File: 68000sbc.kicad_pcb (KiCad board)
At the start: 2 copper layers, 127 x 90.8 mm, 49 parts, among them J1 USB_B, J2 5V FTDI SERIAL, J3 RTC (SparkFun BOB-10160), J4 CFCARD/IDE, J5 EXPANSION (F.Cu), J6 EXPANSION (B.Cu), SW1 RESET, SW2 BTN1, U1 74HC139, U2 74HC14, U3 TMP68HC000P-12, U4 AS6C4008-55PCN, U5 28C256, U6 AS6C4008-55PCN, U7 28C256, U8 TL16C550, X1 12MHz, X2 12MHz

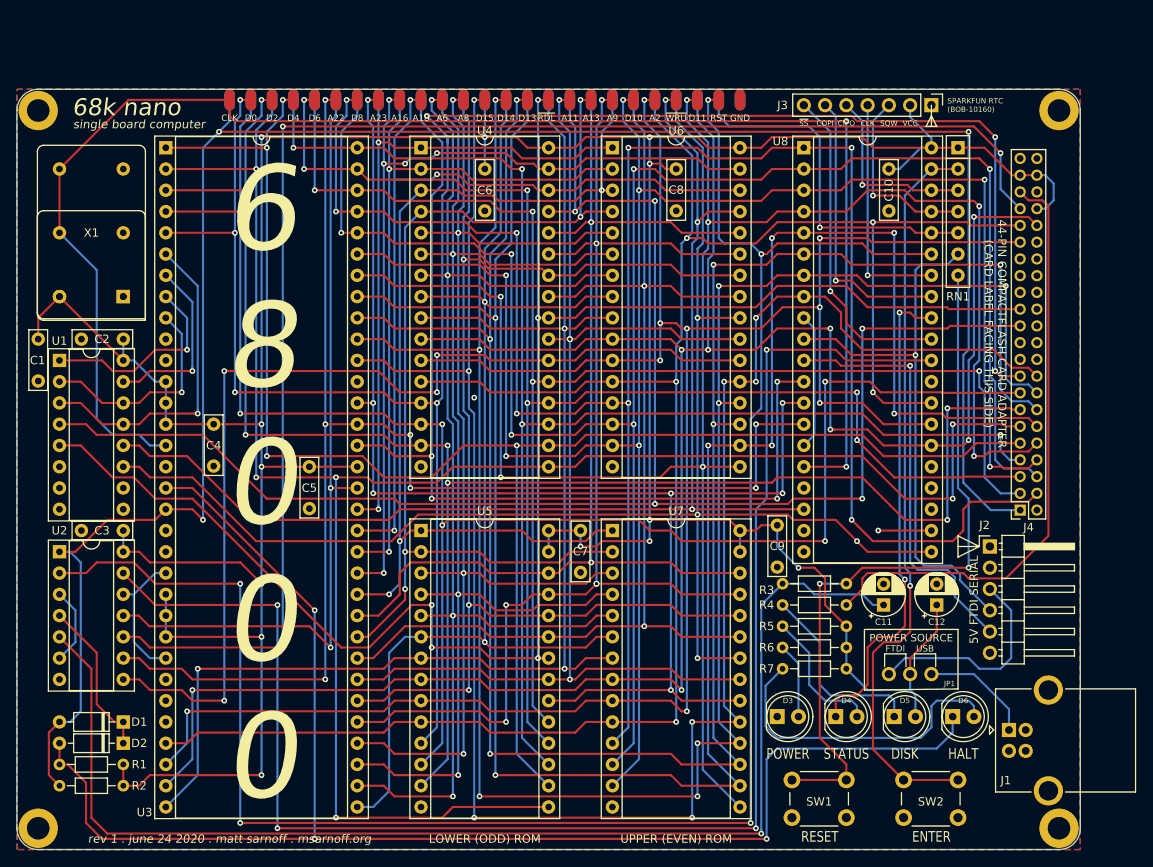
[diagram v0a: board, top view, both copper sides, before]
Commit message: Convert DIP-64 CPU to PGA-68 (MC68HC000RC) on a 4-layer board, fully routed
- New footprint PadRows:MC68HC000_PGA68 (pad numbers = DIP-64 pins, so the
  existing CPU_NXP_68000 symbol works unchanged)
- U3 swapped DIP-64 -> PGA-68; X1/X2 oscillator and J5/J6 headers relocated
  to clear the PGA; top board edge raised 6.4mm
- Board converted to 4 layers: F.Cu/B.Cu signal, In1.Cu GND plane,
  In2.Cu VCC plane (PGA inner-pin escape needs >2 layers)
- Routed with FreeRouting (119/137 nets) + a custom maze router for the
  final 6 spans; DRC: 0 unconnected, 0 copper/electrical violations
- PGA68/ holds the pin map, conversion scripts, and the routing report

Co-Authored-By: Claude Opus 4.8 <noreply@anthropic.com>
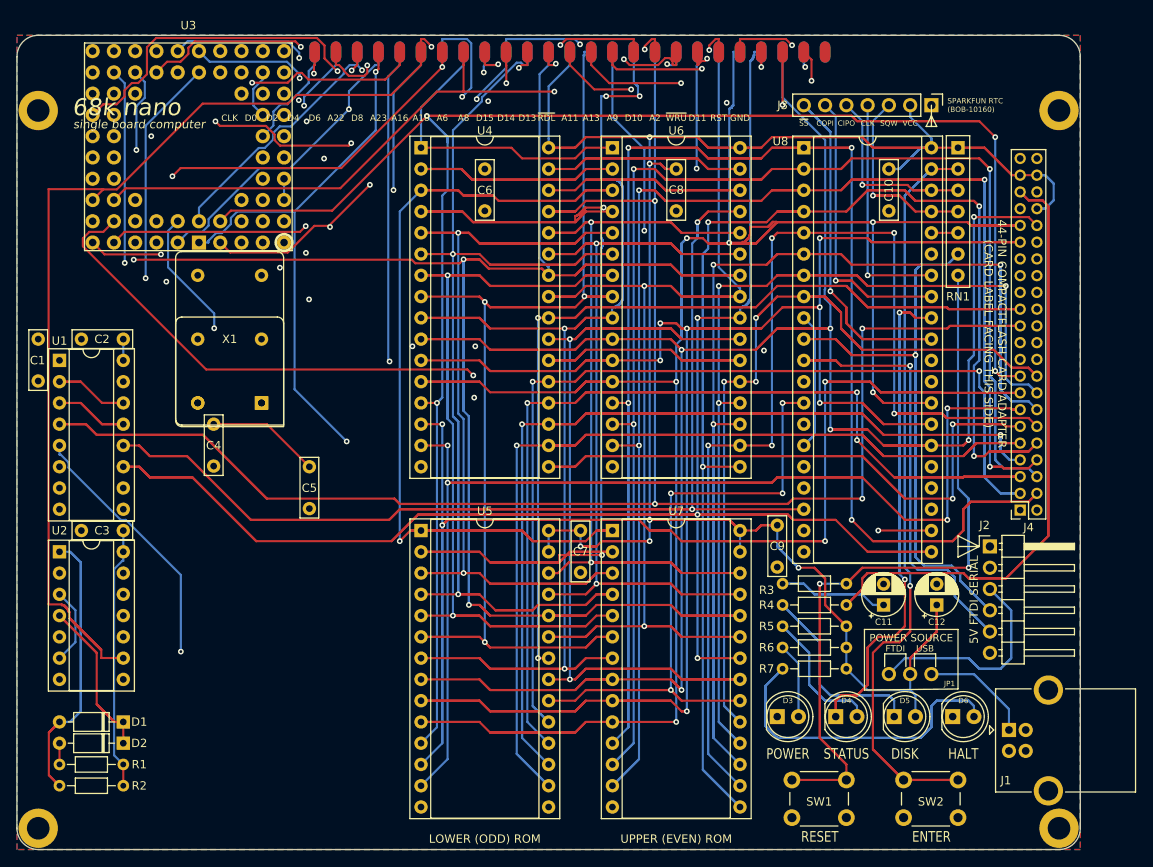
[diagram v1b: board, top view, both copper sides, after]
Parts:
- U3: value TMP68HC000P-12 -> MC68HC000RC10; footprint Package_DIP:DIP-64_W22.86mm_Socket -> PadRows:MC68HC000_PGA68
- moved X1 20.8 mm to (72.4, 76.2)
- moved X2 20.8 mm to (72.4, 76.2)
- moved J5 11.7 mm to (109.2, 38.1)
- moved J6 11.7 mm to (109.2, 30.5)
- moved U3 2.69 mm to (63.6, 45.6)
- renumbered REF** to H1, REF** to H2, REF** to H3, REF** to H4
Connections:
- net /R,~W renamed /R,~{W}
- net /~A20 renamed /~{A20}
- net /~A22 renamed /~{A22}
- net /~AS renamed /~{AS}
- net /~BTN1 renamed /~{BTN1}
- net /~CFLED renamed /~{CFLED}
- net /~HALT renamed /~{HALT}
- net /~IRQ renamed /~{IRQ}
- net /~LDS renamed /~{LDS}
- net /~RDL renamed /~{RDL}
- net /~RDU renamed /~{RDU}
- net /~RESET renamed /~{RESET}
- net /~RESETBTN renamed /~{RESETBTN}
- net /~RTC_SS renamed /~{RTC_SS}
- net /~UDS renamed /~{UDS}
- net /~WRL renamed /~{WRL}
- net /~WRU renamed /~{WRU}
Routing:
- net /A10: track 154.0 -> 288.0 mm, vias 3 -> 4
- net /A2: track 256.3 -> 378.3 mm
- net /A1: track 240.6 -> 352.6 mm, vias 5 -> 6
- net /A11: track 142.7 -> 251.9 mm, vias 4 -> 6
- net /D5: track 169.9 -> 277.6 mm, vias 4 -> 3
- net /D11: track 230.8 -> 337.5 mm, vias 7 -> 5
- net /A3: track 260.8 -> 363.2 mm, vias 8 -> 7
- net /~{WRL}: track 202.4 -> 303.4 mm, vias 5 -> 4
- net /D7: track 171.5 -> 272.3 mm
- net /A15: track 116.5 -> 216.1 mm, vias 3 -> 2
- net /A14: track 130.6 -> 225.0 mm, vias 2 -> 3
- net /D10: track 225.6 -> 319.2 mm, vias 7 -> 6
- net /A13: track 119.7 -> 212.6 mm, vias 4 -> 5
- net /D8: track 244.3 -> 336.6 mm, vias 8 -> 6
- net /A12: track 136.2 -> 226.3 mm, vias 2 -> 3
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- added copper zone on In1.Cu, net GND
- added copper zone on In2.Cu, net VCC
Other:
- board size 127 x 90.8 mm -> 127 x 97.2 mm
- copper layers 2 -> 4
- net class Default removed
- net class Thicc removed
- board text added: "~{BGACK}"
- board text added: "~{BG}"
- board text added: "~{BR}"
- board text added: "~{DTACK}"
- board text added: "~{DTACK} GROUNDED!!"
- board text added: "~{RDL}"
- board text added: "~{RDU}"
- board text added: "~{RST}"
- board text added: "~{SS}"
- board text added: "~{WRL}"
- board text added: "~{WRU}"
- board text removed: "6 8 0 0 0"
- board text removed: "E"
- board text removed: "FC0"
- board text removed: "FC1"
- board text removed: "FC2"
- board text removed: "NOW IS THE TIME TO THE 68000 HEART ON FIRE!"
- board text removed: "R/~W"
- board text removed: "rev 1 . june 24 2020 . matt sarnoff . msarnoff.org"
- board text removed: "~AS"
- board text removed: "~BERR"
- board text removed: "~BG"
- board text removed: "~BGACK"
- board text removed: "~BR"
- board text removed: "~DTACK"
- board text removed: "~DTACK~ GROUNDED!!"
- board text removed: "~HALT"
- board text removed: "~IPL0"
- board text removed: "~IPL1"
- board text removed: "~IPL2"
- board text removed: "~LDS"
- board text removed: "~RDL"
- board text removed: "~RDU"
- board text removed: "~RESET"
- board text removed: "~RST"
- board text removed: "~SS"
- board text removed: "~UDS"
- board text removed: "~VMA"
- board text removed: "~VPA"
- board text removed: "~WRL"
- board text removed: "~WRU"

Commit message: Make v2 the default board: promote v2 -> 68000sbc.kicad_pcb, v1 -> _v1
Opening the 68000sbc.kicad_pro project now brings up the v2 layout (re-placed,
re-routed, DRC-clean). The previous layout is preserved as 68000sbc_v1.kicad_pcb
for reference. The two project files were identical apart from the embedded
filename field, so the redundant 68000sbc_v2.kicad_pro is dropped and the
canonical 68000sbc.kicad_pro is kept. README board list updated.

Co-Authored-By: Claude Opus 4.8 <noreply@anthropic.com>
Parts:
- moved U3 48.6 mm to (74.5, 93.0)
- moved X1 20.5 mm to (62.8, 58.1)
- moved C5 20.4 mm to (76.0, 63.5)
- moved X2 19.9 mm to (79.5, 57.6)
- moved C4 15.2 mm to (67.0, 63.5)
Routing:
- net /A2: track 378.3 -> 219.4 mm, vias 9 -> 2
- net /A3: track 363.2 -> 220.7 mm, vias 7 -> 1
- net /~{WRL}: track 303.4 -> 163.7 mm, vias 4 -> 1
- net /A1: track 352.6 -> 222.8 mm, vias 6 -> 1
- net /D0: track 298.6 -> 174.9 mm, vias 5 -> 1
- net /D11: track 337.5 -> 217.6 mm, vias 5 -> 2
- net /A10: track 288.0 -> 169.1 mm, vias 4 -> 0
- net VCC: track 525.3 -> 410.9 mm, vias 6 -> 0
- net /D10: track 319.2 -> 205.4 mm, vias 6 -> 1
- net /D1: track 290.1 -> 184.0 mm, vias 6 -> 1
- net /~{CFLED}: track 143.3 -> 58.5 mm
- net /D5: track 277.6 -> 193.1 mm
- net /~{RDU}: track 270.3 -> 187.9 mm
- net /D7: track 272.3 -> 191.1 mm
- net /A15: track 216.1 -> 139.0 mm, vias 2 -> 0
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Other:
- board text added: "MAKE 68000 GREAT AGAIN"
